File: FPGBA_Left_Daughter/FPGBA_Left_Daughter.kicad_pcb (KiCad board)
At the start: 2 copper layers, 38 x 49.5 mm, 9 parts

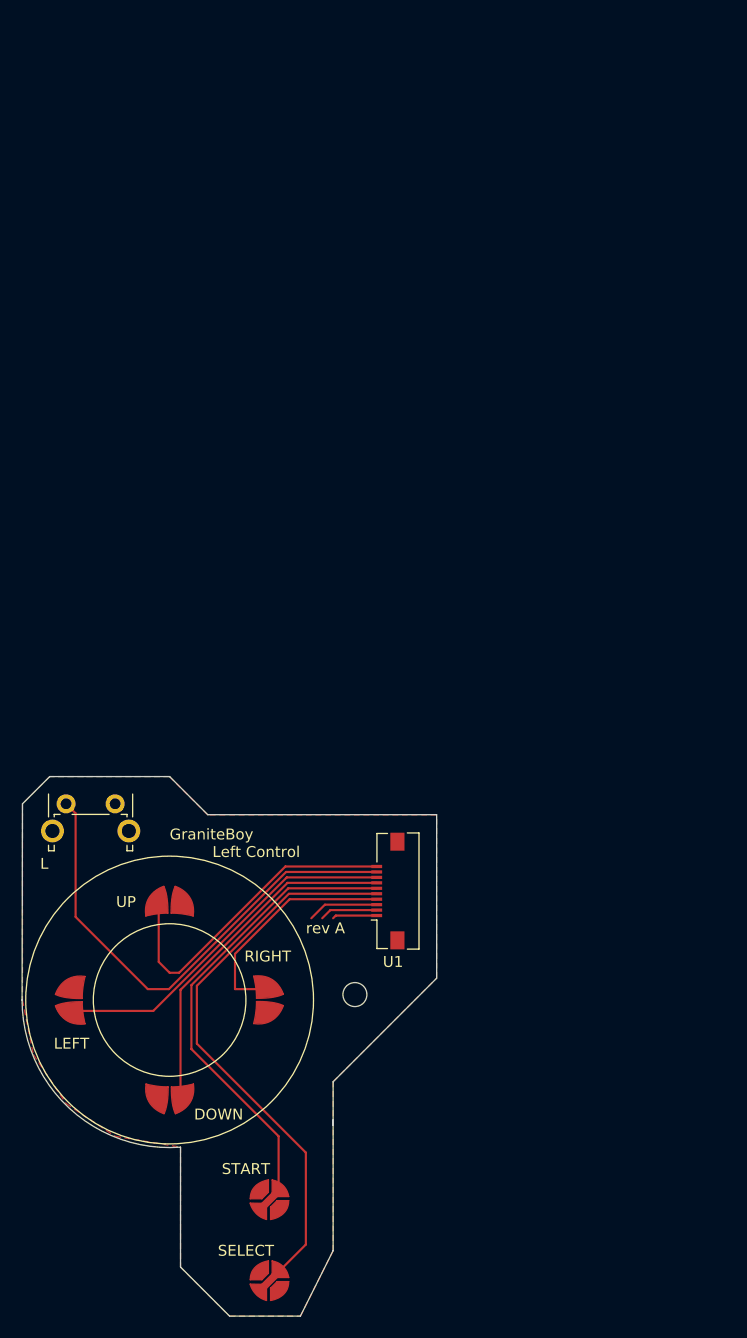
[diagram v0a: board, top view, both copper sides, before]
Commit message: added JTAG + QSPI traces to PCB
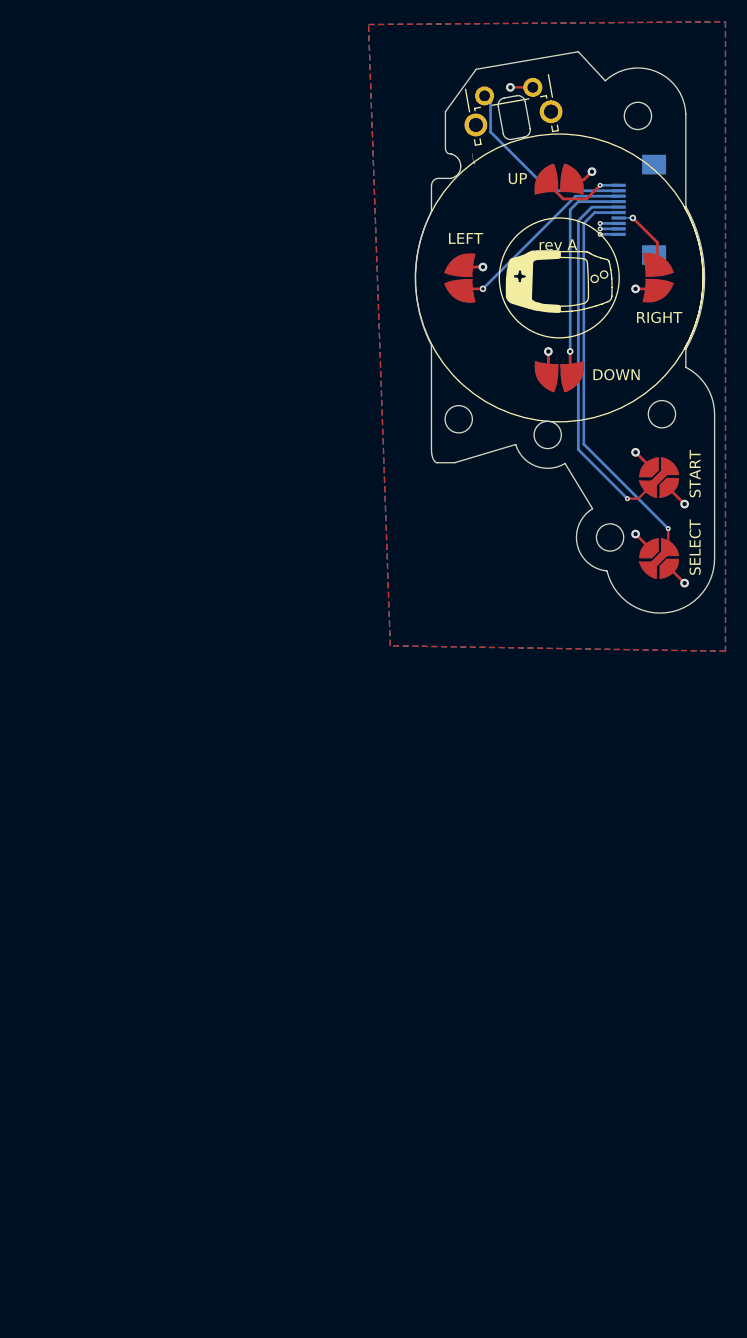
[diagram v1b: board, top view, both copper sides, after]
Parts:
- removed REF**: ▲, MountingHole:MountingHole_2.2mm_M2
- U1: footprint Connector_FFC-FPC:Molex_54548-1071_1x10-1MP_P0.5mm_Horizontal -> Connector_FFC-FPC:Hirose_FH12-10S-0.5SH_1x10-1MP_P0.50mm_Horizontal; moved to B.Cu
- moved SWP9 75.5 mm to (89.4, 70.0), turned to 10 degrees
- moved SWP5 75.3 mm to (83.2, 86.8)
- moved SWP2 75.3 mm to (105.4, 108.2)
- moved SWP3 75.3 mm to (105.4, 100.8)
- moved SWP4 75.3 mm to (109.2, 86.8)
- moved SWP6 75.3 mm to (96.2, 73.8)
- moved SWP7 75.3 mm to (96.2, 99.8)
- moved U1 66.6 mm to (103.5, 80.5), turned to -90 degrees
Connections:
- U1 pad 1: GND -> /P6
- U1 pad 10: /P6 -> GND
- U1 pad 2: GND -> /P9
- U1 pad 3: GND -> /P5
- U1 pad 4: /P4 -> /P7
- U1 pad 5: /P2 -> /P3
- U1 pad 6: /P3 -> /P2
- U1 pad 7: /P7 -> /P4
- U1 pad 8: /P5 -> GND
- U1 pad 9: /P9 -> GND
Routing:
- net /P9: track 45.6 -> 17.5 mm
- net /P6: track 30.0 -> 8.48 mm, vias 0 -> 1
- net /P5: track 33.1 -> 18.0 mm, vias 0 -> 1
- net /P2: track 51.4 -> 36.8 mm, vias 0 -> 1
- net /P4: track 21.3 -> 6.73 mm, vias 0 -> 1
- net /P7: track 32.0 -> 20.0 mm, vias 0 -> 1
- net GND: track 16.3 -> 24.1 mm, vias 0 -> 12
- net /P3: track 42.9 -> 36.5 mm, vias 0 -> 1
- added copper zone on B.Cu, net GND
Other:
- board size 38 x 49.5 mm -> 27.4 x 51.5 mm
- board text added: "DOWN"
- board text added: "LEFT"
- board text added: "RIGHT"
- board text added: "UP"
- board text removed: "GraniteBoy Left Control"
